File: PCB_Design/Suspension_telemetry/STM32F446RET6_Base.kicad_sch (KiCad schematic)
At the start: 28 parts, among them J2 Conn_01x03_Pin, J5 HBHR-B2-10-VG-SMT, U1 STM32F446RET6, Y1 Crystal_GND24_Small, Y2 ABS07-32.768KHZ-9-T

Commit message: pcv v2 finished
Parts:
- removed C21: 0.1u, Capacitor_SMD:C_0603_1608Metric, symbol Device:C_Small
- removed J2: Conn_01x03_Pin, Connector_PinHeader_1.27mm:PinHeader_1x03_P1.27mm_Vertical, symbol Connector:Conn_01x03_Pin
- removed J5: HBHR-B2-10-VG-SMT, HBHRB210VGSMT:HBHRB210VGSMT, symbol HBHR-B2-10-VG-SMT:HBHR-B2-10-VG-SMT
- removed R10: 22, Resistor_SMD:R_0603_1608Metric_Pad0.98x0.95mm_HandSolder, symbol Device:R_Small
- removed S1: 1825965-1, 18259651-switch:18259651, symbol 1825965-1:1825965-1
- added S1: OS102011MA1QN1, MikroP_90:OS102011MA1QN1, symbol MIKRO_P:OS102011MA1QN1
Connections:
- net +3.3V: now also S1.3
- net GND: now also S1.1
- net at R9.1: now also S1.2
- net TRAVEL_SENSOR_FRONT: now reaches U1.10 (PC2)
- net ACCELEROMETER_INT0: now reaches U1.38 (PC7)
- net CHARGE_DETECTION: now reaches U1.50 (PA15)
- net RIGHT_BUTTON: now reaches U1.58 (PB6)
- net LEFT_BUTTON: now reaches U1.59 (PB7)
- net BRAKE_SENSOR_RIGHT: now reaches U1.8 (PC0)
- net BRAKE_SENSOR_LEFT: now reaches U1.9 (PC1)
- net ADC2_IN1 renamed PRESSURE_SENSOR_FRONT
- net ADC2_IN13 renamed TRAVEL_SENOR_REAR
- net ADC2_IN14: no longer names the net of U1.24 (PC4)
- net ADC2_IN4 renamed BATTERY_LEVEL
- net ADC3_IN0: no longer names the net of U1.14 (PA0)
- net PA5: no longer names the net of U1.21 (PA5)
- net PB0: no longer names the net of U1.26 (PB0)
- net USART_RX: no longer names the net of U1.17 (PA3)
- net USART_TX renamed PRESSURE_SENSOR_REAR
- no-connect marks 25 -> 21

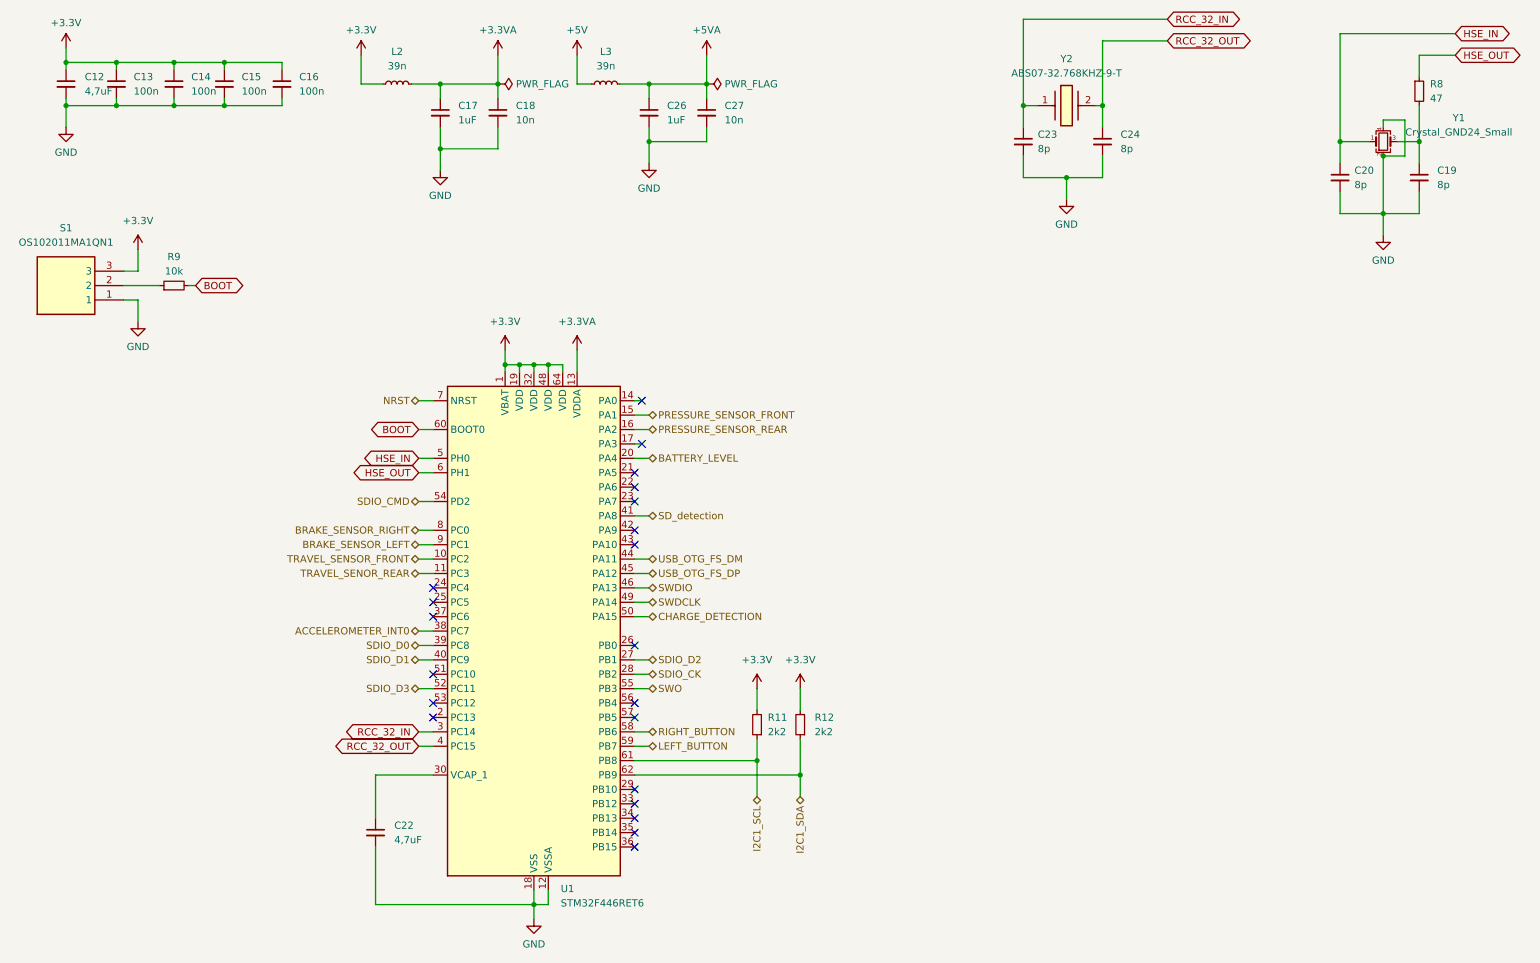
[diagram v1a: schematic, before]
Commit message: adding swnsor mounts
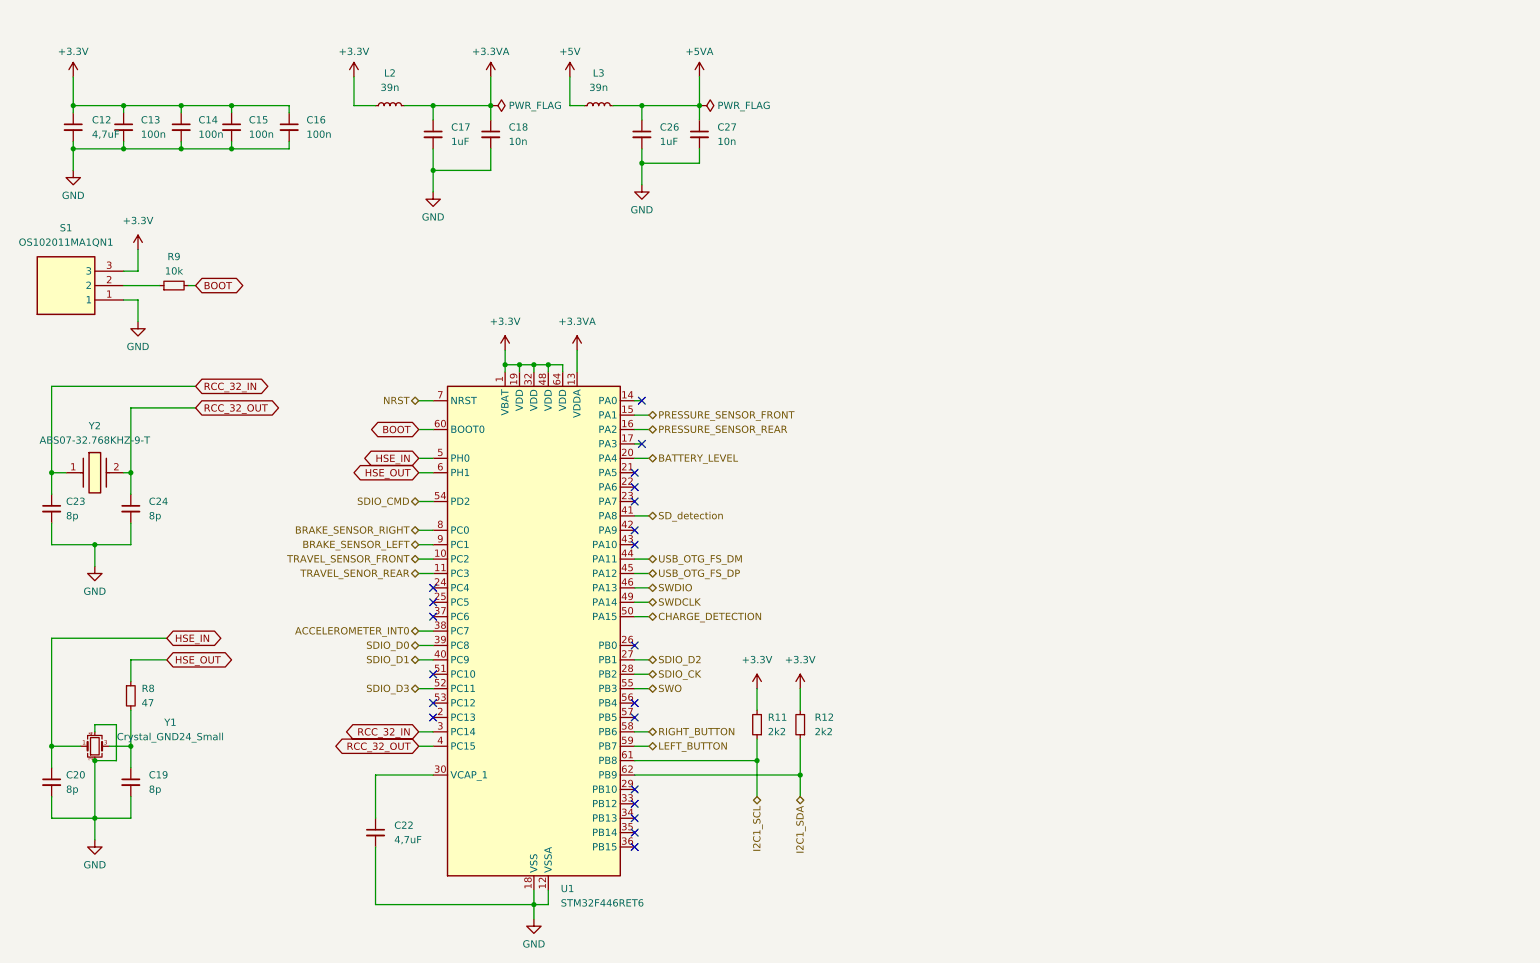
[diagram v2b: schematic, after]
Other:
- moved on the sheet: C12, C13, C14, C15, C16, C17, C18, C19, C20, C23, C24, C26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
